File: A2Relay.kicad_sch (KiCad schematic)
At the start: 7 parts, among them J1 Gameport, J2 Gamepad, J3 /RESET, J4 RELAY, U1 SN74ALS259, U2 SN74ALS259DR

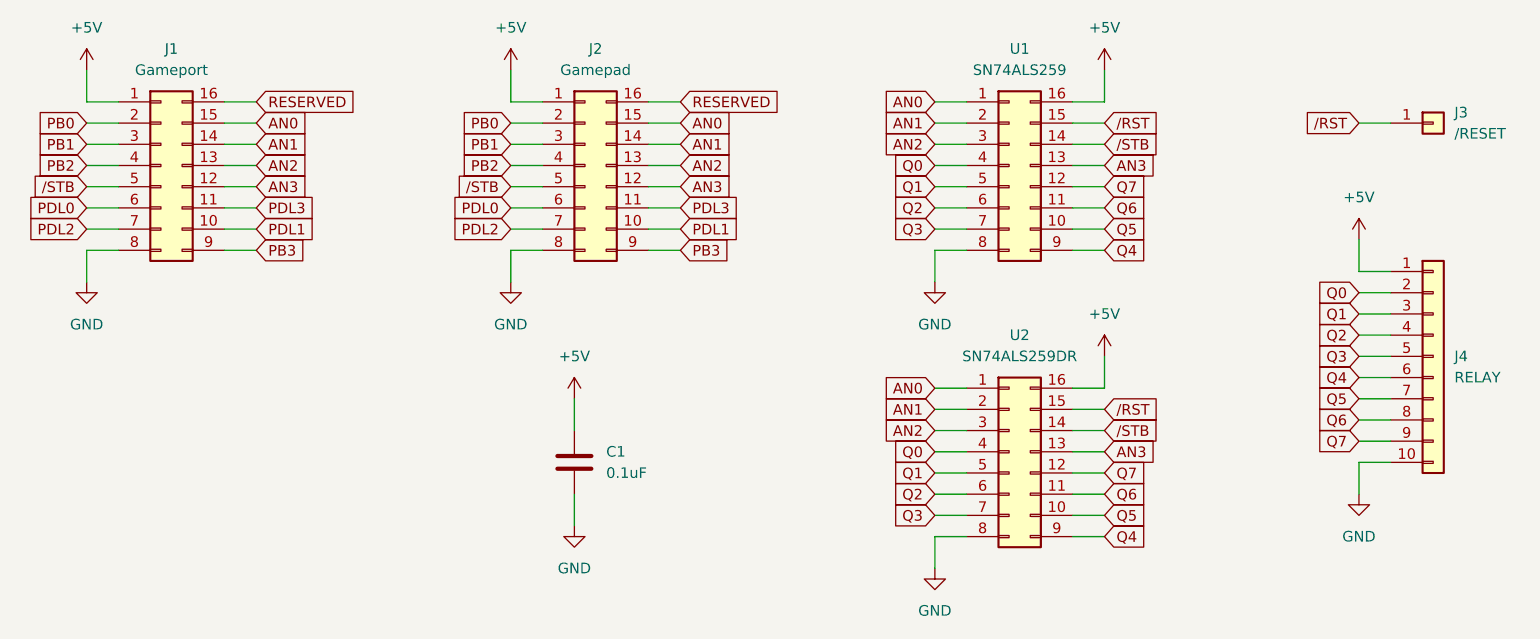
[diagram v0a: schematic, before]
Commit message: Update to KiCad 9.0, add surface mount capacitor, swap VCC / GND on relay connector
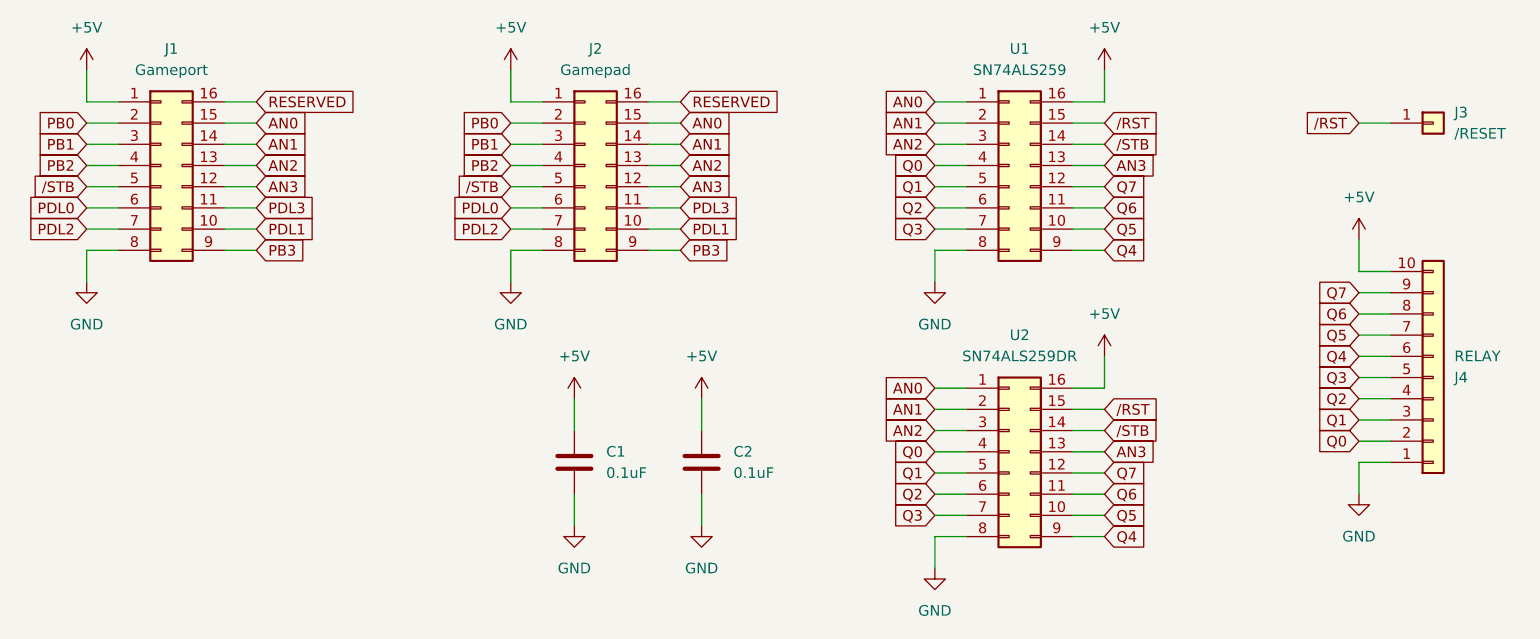
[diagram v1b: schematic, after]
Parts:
- added C2: 0.1uF, Capacitor_SMD:C_0603_1608Metric_Pad1.08x0.95mm_HandSolder, symbol Device:C
- C1: footprint Capacitor_THT:C_Disc_D3.0mm_W1.6mm_P2.50mm -> Capacitor_THT:C_Disc_D4.3mm_W1.9mm_P5.00mm
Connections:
- net +5V: now also J4.10 (Pin_10), C2.1; no longer J4.1 (Pin_1)
- net GND: now also J4.1 (Pin_1), C2.2; no longer J4.10 (Pin_10)
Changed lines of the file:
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@@
 (kicad_sch
-	(version 20231120)
+	(version 20250114)
 	(generator "eeschema")
-	(generator_version "8.0")
+	(generator_version "9.0")
 	(paper "A4")
 	(wire
@@
 	(wire
 		(pts
-			(xy 193.04 67.31) (xy 196.85 67.31)
+			(xy 193.04 85.09) (xy 196.85 85.09)
 		)
 		(stroke
@@
 	(wire
 		(pts
-			(xy 193.04 77.47) (xy 196.85 77.47)
+			(xy 193.04 74.93) (xy 196.85 74.93)
 		)
 		(stroke
@@
 	(wire
 		(pts
-			(xy 193.04 82.55) (xy 196.85 82.55)
+			(xy 193.04 69.85) (xy 196.85 69.85)
 		)
 		(stroke
@@
 	(wire
 		(pts
-			(xy 193.04 69.85) (xy 196.85 69.85)
+			(xy 193.04 82.55) (xy 196.85 82.55)
 		)
 		(stroke
@@
 	(wire
 		(pts
-			(xy 193.04 80.01) (xy 196.85 80.01)
+			(xy 193.04 72.39) (xy 196.85 72.39)
 		)
 		(stroke
@@
 	(wire
 		(pts
+			(xy 114.3 95.25) (xy 114.3 91.44)
+		)
+		(stroke
+			(width 0)
+			(type default)
+		)
+	)
+	(wire
+		(pts
 			(xy 91.44 40.64) (xy 91.44 44.45)
 		)
@@
 	(wire
 		(pts
-			(xy 193.04 74.93) (xy 196.85 74.93)
+			(xy 114.3 80.01) (xy 114.3 83.82)
+		)
+		(stroke
+			(width 0)
+			(type default)
+		)
+	)
+	(wire
+		(pts
+			(xy 193.04 77.47) (xy 196.85 77.47)
 		)
 		(stroke
@@
 	(wire
 		(pts
-			(xy 193.04 85.09) (xy 196.85 85.09)
+			(xy 193.04 67.31) (xy 196.85 67.31)
 		)
 		(stroke
@@
 	(wire
 		(pts
-			(xy 193.04 72.39) (xy 196.85 72.39)
+			(xy 193.04 80.01) (xy 196.85 80.01)
 		)
 		(stroke
@@
 	(global_label "Q2"
 		(shape input)
-		(at 193.04 72.39 180)
+		(at 193.04 80.01 180)
 		(fields_autoplaced yes)
 		(effects
@@
 		)
 		(property "Intersheetrefs" "${INTERSHEET_REFS}"
-			(at 187.5148 72.39 0)
+			(at 187.5148 80.01 0)
 			(effects
 				(font
@@
 	(global_label "Q0"
 		(shape input)
-		(at 193.04 67.31 180)
+		(at 193.04 85.09 180)
 		(fields_autoplaced yes)
 		(effects
@@
 		)
 		(property "Intersheetrefs" "${INTERSHEET_REFS}"
-			(at 187.5148 67.31 0)
+			(at 187.5148 85.09 0)
 			(effects
 				(font
@@
 	(global_label "Q4"
 		(shape input)
-		(at 193.04 77.47 180)
+		(at 193.04 74.93 180)
 		(fields_autoplaced yes)
 		(effects
@@
 		)
 		(property "Intersheetrefs" "${INTERSHEET_REFS}"
-			(at 187.5148 77.47 0)
+			(at 187.5148 74.93 0)
 			(effects
 				(font
@@
 	(global_label "Q6"
 		(shape input)
-		(at 193.04 82.55 180)
+		(at 193.04 69.85 180)
 		(fields_autoplaced yes)
 		(effects
@@
 		)
 		(property "Intersheetrefs" "${INTERSHEET_REFS}"
-			(at 187.5148 82.55 0)
+			(at 187.5148 69.85 0)
 			(effects
 				(font
@@
 	(global_label "Q5"
 		(shape input)
-		(at 193.04 80.01 180)
+		(at 193.04 72.39 180)
 		(fields_autoplaced yes)
 		(effects
@@
 		)
 		(property "Intersheetrefs" "${INTERSHEET_REFS}"
-			(at 187.5148 80.01 0)
+			(at 187.5148 72.39 0)
 			(effects
 				(font
@@
 	(global_label "Q1"
 		(shape input)
-		(at 193.04 69.85 180)
+		(at 193.04 82.55 180)
 		(fields_autoplaced yes)
 		(effects
@@
 		)
 		(property "Intersheetrefs" "${INTERSHEET_REFS}"
-			(at 187.5148 69.85 0)
+			(at 187.5148 82.55 0)
 			(effects
 				(font
@@
 	(global_label "Q7"
 		(shape input)
-		(at 193.04 85.09 180)
+		(at 193.04 67.31 180)
 		(fields_autoplaced yes)
 		(effects
@@
 		)
 		(property "Intersheetrefs" "${INTERSHEET_REFS}"
-			(at 187.5148 85.09 0)
+			(at 187.5148 67.31 0)
 			(effects
 				(font
@@
 	(global_label "Q3"
 		(shape input)
-		(at 193.04 74.93 180)
+		(at 193.04 77.47 180)
 		(fields_autoplaced yes)
 		(effects
@@
 		)
 		(property "Intersheetrefs" "${INTERSHEET_REFS}"
-			(at 187.5148 74.93 0)
+			(at 187.5148 77.47 0)
 			(effects
 				(font
@@
 	)
 	(symbol
+		(lib_id "power:+5V")
+		(at 114.3 80.01 0)
+		(unit 1)
+		(exclude_from_sim no)
+		(in_bom yes)
+		(on_board yes)
+		(dnp no)
+		(fields_autoplaced yes)
+		(property "Reference" "#PWR013"
+			(at 114.3 83.82 0)
+			(effects
+				(font
+					(size 1.27 1.27)
+				)
+				(hide yes)
+			)
+		)
+		(property "Value" "+5V"
+			(at 114.3 74.93 0)
+			(effects
+				(font
+					(size 1.27 1.27)
+				)
+			)
+		)
+		(property "Footprint" ""
+			(at 114.3 80.01 0)
+			(effects
+				(font
+					(size 1.27 1.27)
+				)
+				(hide yes)
+			)
+		)
+		(property "Datasheet" ""
+			(at 114.3 80.01 0)
+			(effects
+				(font
+					(size 1.27 1.27)
+				)
+				(hide yes)
+			)
+		)
+		(property "Description" "Power symbol creates a global label with name \"+5V\""
+			(at 114.3 80.01 0)
+			(effects
+				(font
+					(size 1.27 1.27)
+				)
+				(hide yes)
+			)
+		)
+		(pin "1"
+		)
+		(instances
+			(project "A2Relay"
+				(path "/e2070a63-a94a-4866-9db3-3eab77b7b598"
+					(reference "#PWR013")
+					(unit 1)
+				)
+			)
+		)
+	)
+	(symbol
+		(lib_id "power:GND")
+		(at 114.3 95.25 0)
+		(unit 1)
+		(exclude_from_sim no)
+		(in_bom yes)
+		(on_board yes)
+		(dnp no)
+		(fields_autoplaced yes)
+		(property "Reference" "#PWR014"
+			(at 114.3 101.6 0)
+			(effects
+				(font
+					(size 1.27 1.27)
+				)
+				(hide yes)
+			)
+		)
+		(property "Value" "GND"
+			(at 114.3 100.33 0)
+			(effects
+				(font
+					(size 1.27 1.27)
+				)
+			)
+		)
+		(property "Footprint" ""
+			(at 114.3 95.25 0)
+			(effects
+				(font
+					(size 1.27 1.27)
+				)
+				(hide yes)
+			)
+		)
+		(property "Datasheet" ""
+			(at 114.3 95.25 0)
+			(effects
+				(font
+					(size 1.27 1.27)
+				)
+				(hide yes)
+			)
+		)
+		(property "Description" "Power symbol creates a global label with name \"GND\" , ground"
+			(at 114.3 95.25 0)
+			(effects
+				(font
+					(size 1.27 1.27)
+				)
+				(hide yes)
+			)
+		)
+		(pin "1"
+		)
+		(instances
+			(project "A2Relay"
+				(path "/e2070a63-a94a-4866-9db3-3eab77b7b598"
+					(reference "#PWR014")
+					(unit 1)
+				)
+			)
+		)
+	)
+	(symbol
 		(lib_id "Connector_Generic:Conn_02x08_Counter_Clockwise")
 		(at 151.13 86.36 0)
@@
 			)
 		)
-		(property "Footprint" "Capacitor_THT:C_Disc_D3.0mm_W1.6mm_P2.50mm"
+		(property "Footprint" "Capacitor_THT:C_Disc_D4.3mm_W1.9mm_P5.00mm"
 			(at 100.0252 91.44 0)
 			(effects
@@
 	)
 	(symbol
-		(lib_id "Connector_Generic:Conn_01x10")
-		(at 201.93 74.93 0)
+		(lib_id "Device:C")
+		(at 114.3 87.63 0)
 		(unit 1)
 		(exclude_from_sim no)
@@
 		(dnp no)
 		(fields_autoplaced yes)
+		(property "Reference" "C2"
+			(at 118.11 86.3599 0)
+			(effects
+				(font
+					(size 1.27 1.27)
+				)
+				(justify left)
+			)
+		)
+		(property "Value" "0.1uF"
+			(at 118.11 88.8999 0)
+			(effects
+				(font
+					(size 1.27 1.27)
+				)
+				(justify left)
+			)
+		)
+		(property "Footprint" "Capacitor_SMD:C_0603_1608Metric_Pad1.08x0.95mm_HandSolder"
+			(at 115.2652 91.44 0)
+			(effects
+				(font
+					(size 1.27 1.27)
+				)
+				(hide yes)
+			)
+		)
+		(property "Datasheet" "~"
+			(at 114.3 87.63 0)
+			(effects
+				(font
+					(size 1.27 1.27)
+				)
+				(hide yes)
+			)
+		)
+		(property "Description" "Unpolarized capacitor"
+			(at 114.3 87.63 0)
+			(effects
+				(font
+					(size 1.27 1.27)
+				)
+				(hide yes)
+			)
+		)
+		(pin "1"
+		)
+		(pin "2"
+		)
+		(instances
+			(project "A2Relay"
+				(path "/e2070a63-a94a-4866-9db3-3eab77b7b598"
+					(reference "C2")
+					(unit 1)
+				)
+			)
+		)
+	)
+	(symbol
+		(lib_id "Connector_Generic:Conn_01x10")
+		(at 201.93 77.47 0)
+		(mirror x)
+		(unit 1)
+		(exclude_from_sim no)
+		(in_bom yes)
+		(on_board yes)
+		(dnp no)
 		(property "Reference" "J4"
-			(at 204.47 74.9299 0)
+			(at 204.47 77.4701 0)
 			(effects
 				(font
@@
 		)
 		(property "Value" "RELAY"
-			(at 204.47 77.4699 0)
+			(at 204.47 74.9301 0)
 			(effects
 				(font
@@
 		)
 		(property "Footprint" "Connector_PinHeader_2.54mm:PinHeader_1x10_P2.54mm_Vertical"
-			(at 201.93 74.93 0)
+			(at 201.93 77.47 0)
 			(effects
 				(font
@@
 		)
 		(property "Datasheet" "~"
-			(at 201.93 74.93 0)
+			(at 201.93 77.47 0)
 			(effects
 				(font
@@
 		)
 		(property "Description" "Generic connector, single row, 01x10, script generated (kicad-library-utils/schlib/autogen/connector/)"
-			(at 201.93 74.93 0)
+			(at 201.93 77.47 0)
 			(effects
 				(font
@@
 		)
 	)
+	(embedded_fonts no)
 )
